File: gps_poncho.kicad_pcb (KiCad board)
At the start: 2 copper layers, 85.7 x 60.3 mm, 5 parts

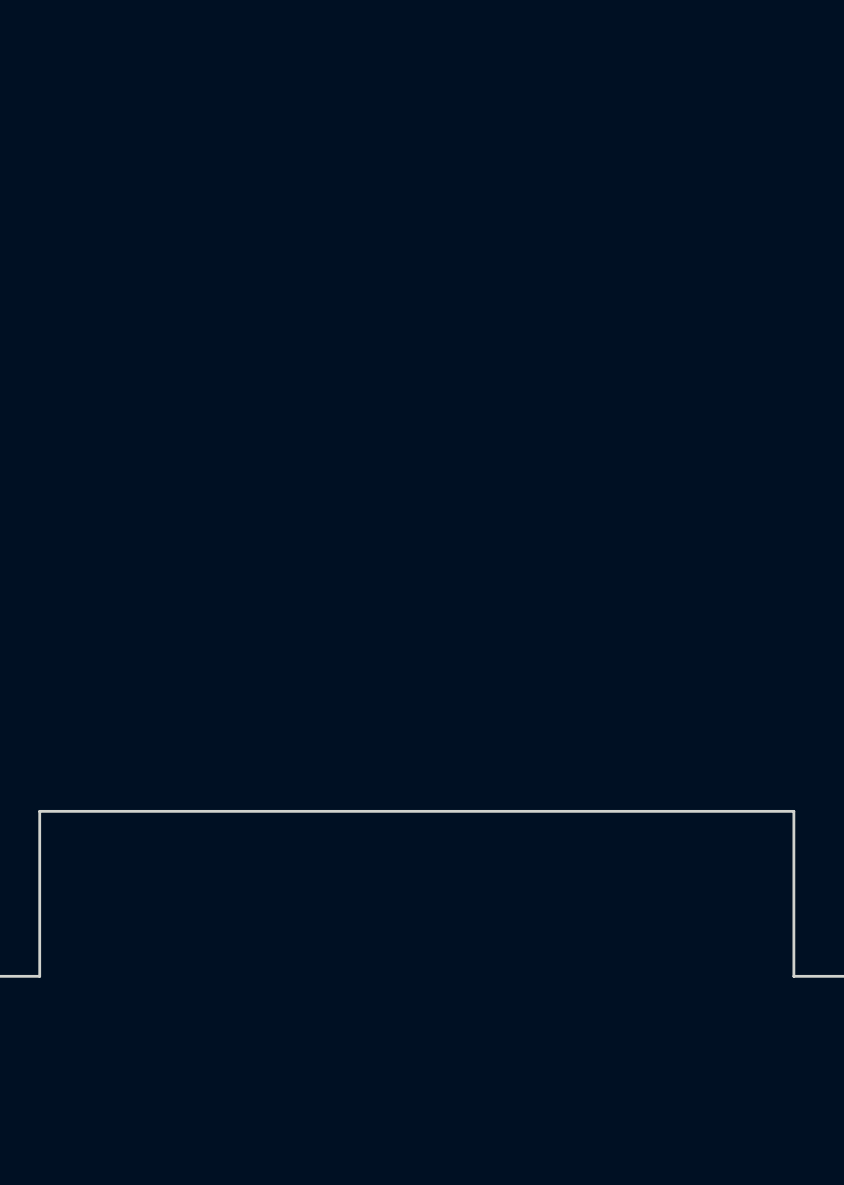
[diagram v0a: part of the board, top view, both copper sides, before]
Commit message: Se añaden footprints y se toma en cuenta revisión de Victor Stalla. Se cambia slot de sd card
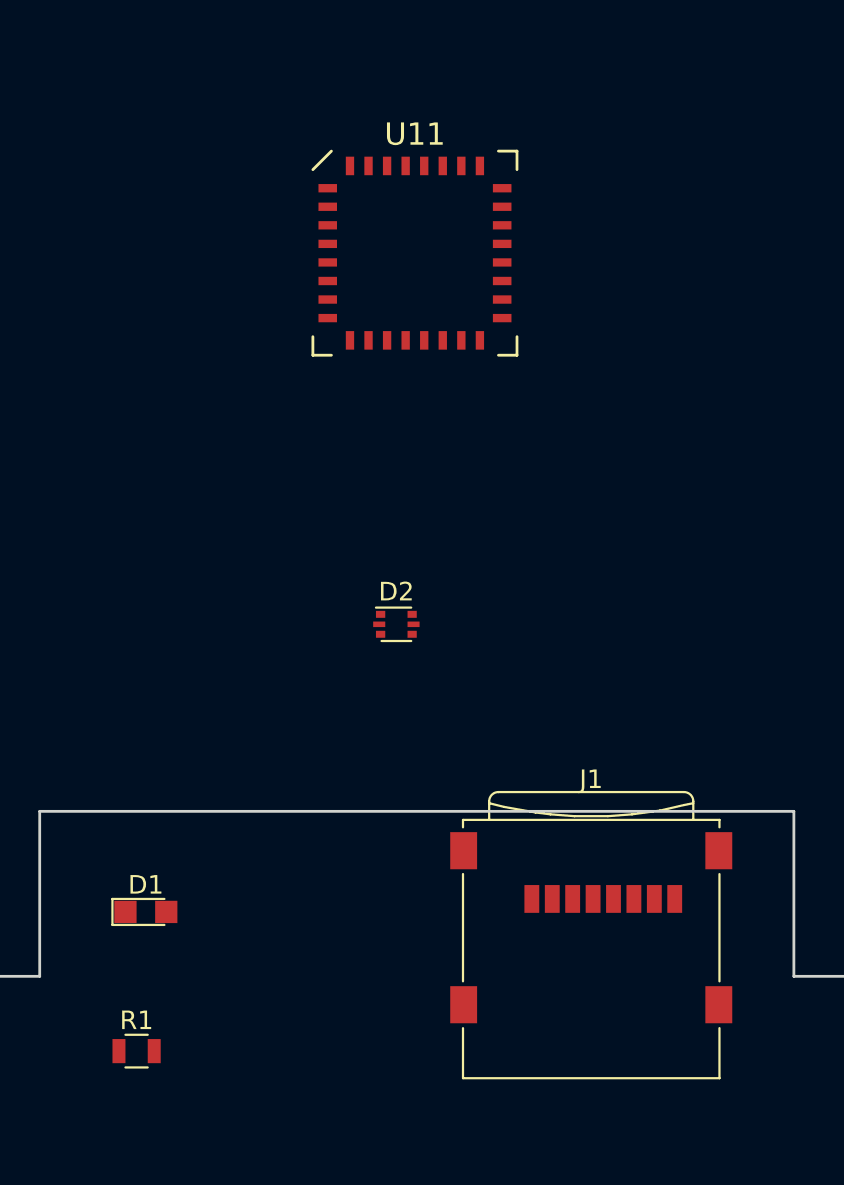
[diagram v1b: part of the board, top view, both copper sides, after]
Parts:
- added D1: LED Green, footprint:LED_0805, F.Cu at (87.0, 137.5)
- added D2: PESD3V3L5UV, footprint:sot666, F.Cu at (100.5, 122.0)
- added J1: Micro_SD_Card, footprint:microSD_Card_Receptacle_Wuerth_693072010801, F.Cu at (111.0, 139.5)
- added R1: 68, footprint:R_0805, F.Cu at (86.5, 145.0)
- added U11: SE868K3-A, footprint:se868A, F.Cu at (101.5, 102.0)
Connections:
- XA101 pad 1: +3.3VP -> +3V3
- XA101 pad 10: GNDA -> Net-(XA101-Pad10)
- XA101 pad 11: (no net) -> Net-(XA101-Pad11)
- XA101 pad 12: GNDA -> Net-(XA101-Pad12)
- XA101 pad 13: (no net) -> Net-(XA101-Pad13)
- XA101 pad 14: GNDA -> Net-(XA101-Pad14)
- XA101 pad 15: (no net) -> Net-(XA101-Pad15)
- XA101 pad 16: GNDA -> Net-(XA101-Pad16)
- XA101 pad 17: (no net) -> Net-(XA101-Pad17)
- XA101 pad 18: GNDA -> Net-(XA101-Pad18)
- XA101 pad 19: (no net) -> Net-(XA101-Pad19)
- XA101 pad 21: (no net) -> Net-(XA101-Pad21)
- XA101 pad 23: (no net) -> Net-(XA101-Pad23)
- XA101 pad 25: (no net) -> Net-(XA101-Pad25)
- XA101 pad 27: (no net) -> Net-(XA101-Pad27)
- XA101 pad 29: (no net) -> Net-(XA101-Pad29)
- XA101 pad 3: (no net) -> Net-(XA101-Pad3)
- XA101 pad 31: (no net) -> Net-(XA101-Pad31)
- XA101 pad 33: (no net) -> Net-(XA101-Pad33)
- XA101 pad 34: (no net) -> Net-(XA101-Pad34)
- XA101 pad 35: (no net) -> Net-(XA101-Pad35)
- XA101 pad 36: (no net) -> Net-(XA101-Pad36)
- XA101 pad 37: (no net) -> Net-(XA101-Pad37)
- XA101 pad 39: (no net) -> Net-(XA101-Pad39)
- XA101 pad 42: +5V -> +5VP
- XA101 pad 44: (no net) -> Net-(XA101-Pad44)
- XA101 pad 46: (no net) -> Net-(XA101-Pad46)
- XA101 pad 48: (no net) -> Net-(XA101-Pad48)
- XA101 pad 49: (no net) -> Net-(XA101-Pad49)
- XA101 pad 5: (no net) -> Net-(XA101-Pad5)
- XA101 pad 50: (no net) -> Net-(XA101-Pad50)
- XA101 pad 52: (no net) -> Net-(XA101-Pad52)
- XA101 pad 54: (no net) -> Net-(XA101-Pad54)
- XA101 pad 55: (no net) -> Net-(XA101-Pad55)
- XA101 pad 56: (no net) -> Net-(XA101-Pad56)
- XA101 pad 58: (no net) -> /SPI_MISO
- XA101 pad 6: (no net) -> Net-(XA101-Pad6)
- XA101 pad 60: (no net) -> /SPI_CLK
- XA101 pad 61: (no net) -> /SPI_MOSI
- XA101 pad 62: (no net) -> Net-(XA101-Pad62)
- XA101 pad 63: (no net) -> Net-(XA101-Pad63)
- XA101 pad 64: (no net) -> Net-(XA101-Pad64)
- XA101 pad 66: (no net) -> Net-(XA101-Pad66)
- XA101 pad 68: (no net) -> Net-(XA101-Pad68)
- XA101 pad 69: (no net) -> Net-(XA101-Pad69)
- XA101 pad 7: GNDA -> Net-(XA101-Pad7)
- XA101 pad 70: (no net) -> Net-(XA101-Pad70)
- XA101 pad 71: (no net) -> Net-(XA101-Pad71)
- XA101 pad 72: (no net) -> /SD_CARD_CS
- XA101 pad 73: (no net) -> Net-(XA101-Pad73)
- XA101 pad 74: (no net) -> Net-(U11-Pad19)
- XA101 pad 75: (no net) -> Net-(XA101-Pad75)
- XA101 pad 76: (no net) -> Net-(XA101-Pad76)
- XA101 pad 78: (no net) -> Net-(XA101-Pad78)
- XA101 pad 8: GNDA -> Net-(XA101-Pad8)
- XA101 pad 80: (no net) -> Net-(XA101-Pad80)
- XA101 pad 9: (no net) -> Net-(XA101-Pad9)

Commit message: Primera version de PCB
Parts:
- removed MP?: Plantilla_EDU-CIAA, footprint:Plantilla_EDU-CIAA
- moved R1 63.4 mm to (72.0, 83.2), turned to 270 degrees
- moved G*** 61.3 mm to (112.8, 89.0)
- moved J1 57.7 mm to (85.0, 88.0)
- moved D1 55.2 mm to (75.5, 83.5), turned to 90 degrees
- moved G101 46.1 mm to (83.2, 122.5)
- moved G*** 45.8 mm to (94.8, 116.2)
- moved D2 34.9 mm to (97.0, 87.2), turned to 180 degrees
- moved U11 15.2 mm to (113.0, 112.0)
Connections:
- R1 pad 2: +3V3 -> +3.3VP
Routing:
- net /SPI_MOSI: track 0.00 -> 160.5 mm, vias 0 -> 5
- net +3.3VP: track 0.00 -> 124.7 mm, vias 0 -> 7
- net /SPI_CLK: track 0.00 -> 97.1 mm, vias 0 -> 3
- net /SPI_MISO: track 0.00 -> 96.1 mm, vias 0 -> 1
- net /SD_CARD_CS: track 0.00 -> 60.7 mm
- net Net-(U11-Pad19): track 0.00 -> 54.7 mm, vias 0 -> 2
- net GND: track 0.00 -> 15.0 mm, vias 0 -> 1
- net Net-(D1-Pad2): track 0.00 -> 3.54 mm
- added copper zone on B.Cu, net GND
- added copper zone on F.Cu, net GND
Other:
- net class Default: clearance 0.51 -> 0.2
- rule trace_clearance: 0.51 -> 0.2
- board text added: "Diseño dos capas Rutas de 15 mils Tener en cuenta los limites de la capacitancia de la proteccion ESD para determinacion de la velocidad maxima del bus SPI"
- board text removed: "Borrar (Footprint MP1) la Plantilla-EDU-CIAA al finalizar el posicionamiento y definido el borde de PCB."
- board text removed: "Diseño simple faz. Sin requerimientos especiales."
- board text removed: "Editar el rótulo"
- board text removed: "Editar este cuadro para reflejar cantidad de capas, si se han realizado cálculos de impedancia o si es relevante para el funcionamiento."
- board text removed: "PONCHO BASICO http://www.proyecto-ciaa.com.ar/"
- board text removed: "Se sugiere colocar Nombre de Poncho y autor en cobre, serigrafía y rótulo."

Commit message: Revision del PCB
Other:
- board text added: "Diseño dos capas Rutas de 15 mils Con una frecuencia de clock en spi de máxima 5MHz no deberían dar problemas la diferencia de longitud entre lineas SPI (MOSI,MISO) respecto a su clock ni el valor de la capacitancia de la proteccion ESD."
- board text removed: "Diseño dos capas Rutas de 15 mils Tener en cuenta los limites de la capacitancia de la proteccion ESD para determinacion de la velocidad maxima del bus SPI"
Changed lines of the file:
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@@
     (links 51)
     (no_connects 0)
-    (area 59.614999 80.569999 145.490001 141.045001)
+    (area 56 15.774999 279.500001 145.750001)
     (thickness 1.6)
     (drawings 18)
@@
   (title_block
     (title "Poncho GPS datalogger")
-    (date 2017-10-31)
+    (date 2017-11-10)
     (rev 1.0)
     (company "Proyecto CIAA - COMPUTADORA INDUSTRIAL ABIERTA ARGENTINA")
@@
   )
   (setup
-    (last_trace_width 0.254)
+    (last_trace_width 0.381)
     (user_trace_width 0.254)
     (user_trace_width 0.6)
@@
   (gr_line (start 145.415 80.645) (end 145.415 140.97) (angle 90) (layer Edge.Cuts) (width 0.15))
   (gr_line (start 59.69 80.645) (end 145.415 80.645) (angle 90) (layer Edge.Cuts) (width 0.15))
-  (gr_text "Diseño dos capas\n\nRutas de 15 mils\n\nTener en cuenta los limites de la capacitancia de la proteccion ESD \npara determinacion de la velocidad maxima del bus SPI\n" (at 194.945 24.13) (layer Dwgs.User)
+  (gr_text "Diseño dos capas\n\nRutas de 15 mils\n\nCon una frecuencia de clock en spi de máxima 5MHz no deberían \ndar problemas la diferencia de longitud entre lineas SPI \n(MOSI,MISO) respecto a su clock \nni el valor de la capacitancia de la proteccion ESD." (at 190.945 31.13) (layer Dwgs.User)
     (effects (font (size 1.5 1.5) (thickness 0.3)) (justify left))
   )
-  (gr_text STACK-UP (at 227.965 19.05) (layer Dwgs.User)
+  (gr_text STACK-UP (at 227.465 19.8) (layer Dwgs.User)
     (effects (font (size 1.5 1.5) (thickness 0.3)))
   )
